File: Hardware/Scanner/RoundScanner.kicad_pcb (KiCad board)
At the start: 4 copper layers, 45 x 42.5 mm, 78 parts, among them J1 I2C ThroughHole, J3 I2C, J4 Interface, Q1 BSS138DW-7-F, U1 OPA2376xxD, U2 NAU7802SGI, U4 OPA2376xxD, U5 TLC59208FIPWR, U6 AS7341-DLGT, U7 AP7312-1833W6-7, X1 4.9152 MHz

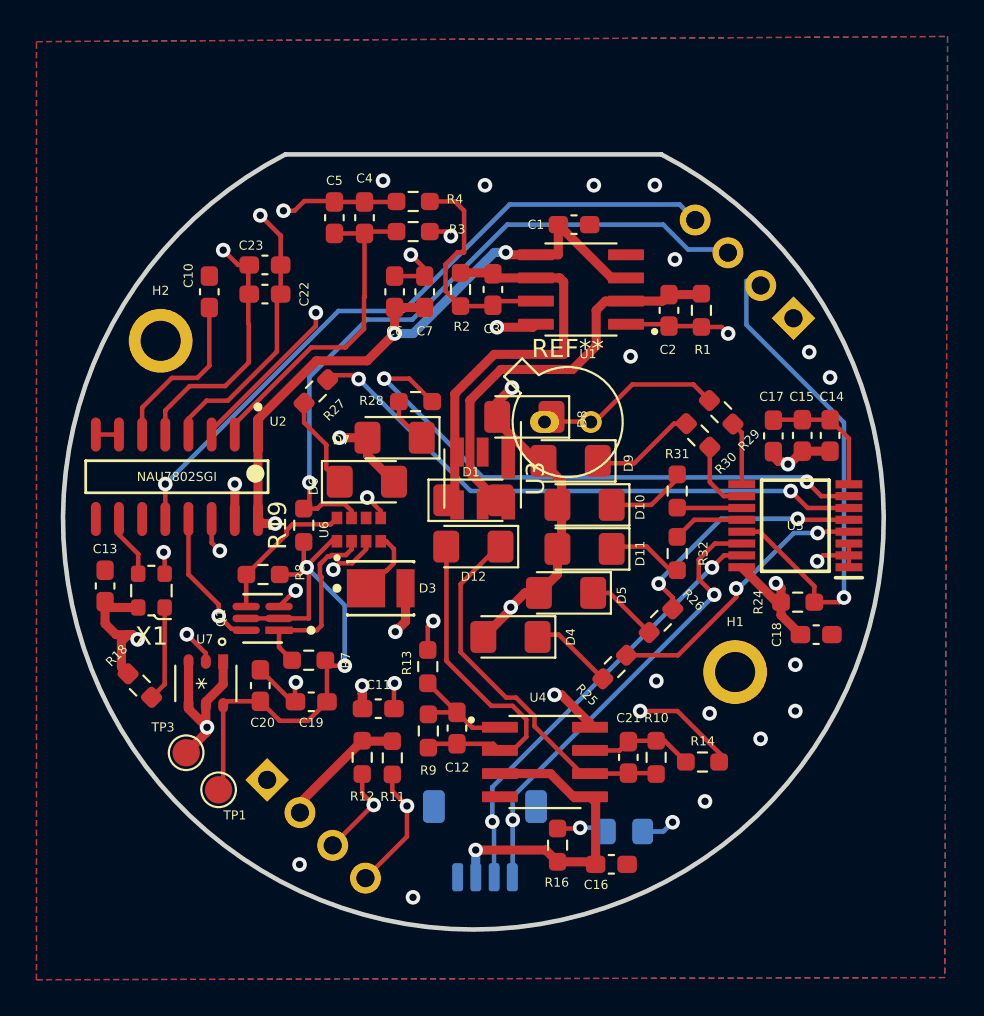
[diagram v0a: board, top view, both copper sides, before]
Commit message: lots of changes, added footprints, fixed broken schemaitcs, fixed kicad 7.0 issues
Signed-off-by: lokimetasmith <lokimail@gmail.com>
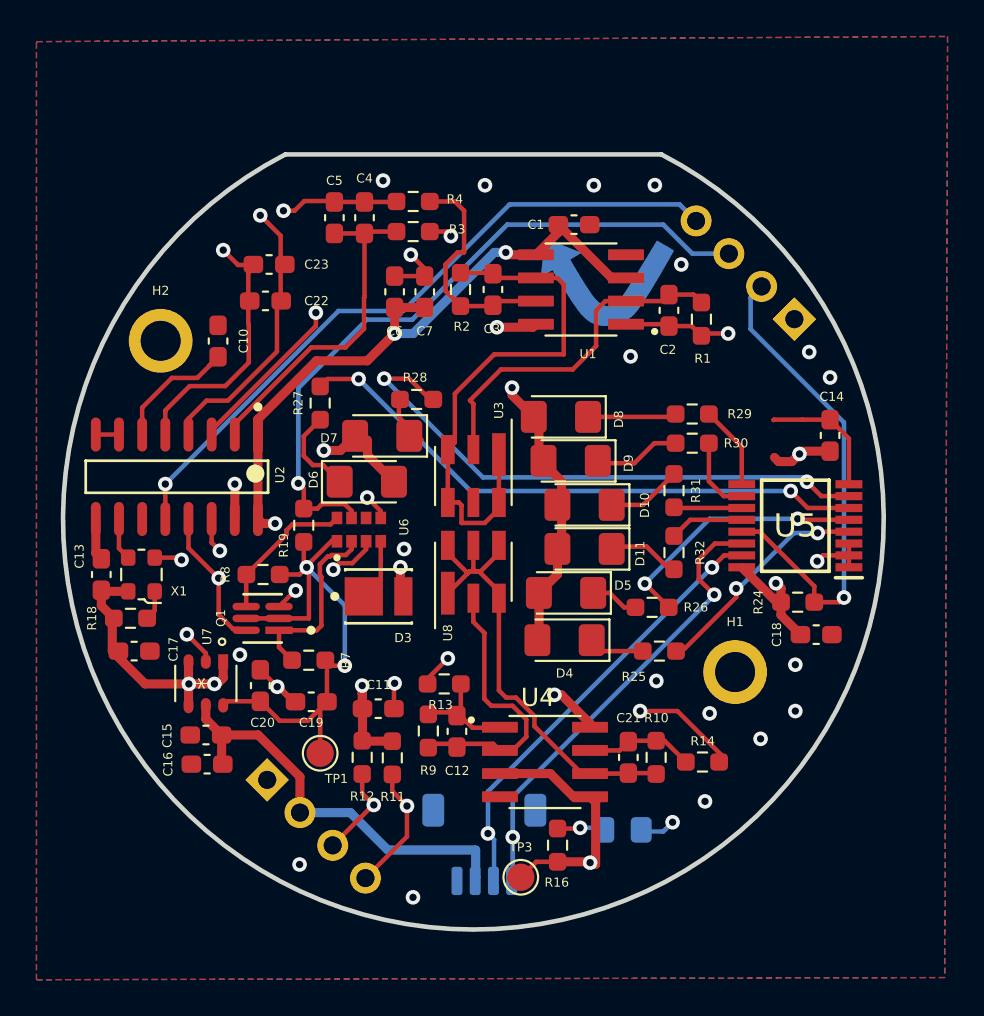
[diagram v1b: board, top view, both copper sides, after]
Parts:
- removed D1, D12: 0090-3111-185, Diode_SMD:D_1206_3216Metric_Pad1.42x1.75mm_HandSolder
- removed REF**: TO-46-2_Window, Package_TO_SOT_THT:TO-46-2_Window
- added U8: ~, MTSM2601SMF1-100:MTSM1346SMF1-100, F.Cu at (89.3, 110.2)
- moved C17 37.0 mm to (70.7, 114.6), turned to 0 degrees
- moved C15 36.6 mm to (74.6, 119.2), turned to 0 degrees
- moved C16 22.8 mm to (74.7, 120.8), turned to 0 degrees
- moved TP3 19.6 mm to (91.9, 127.0)
- moved TP1 5.92 mm to (80.9, 120.2)
- moved R18 3.73 mm to (70.5, 112.8), turned to 180 degrees
- moved D4 2.97 mm to (94.3, 114.0)
- moved C10 2.74 mm to (75.3, 97.6)
- moved R25 2.60 mm to (99.5, 114.6), turned to 180 degrees
- moved D8 2.01 mm to (94.1, 101.7)
- moved R29 1.59 mm to (101.3, 101.6), turned to 180 degrees
- moved R13 1.31 mm to (87.7, 116.4), turned to 180 degrees
- moved X1 1.04 mm to (71.1, 110.4)
- moved R26 0.88 mm to (99.1, 112.2), turned to 180 degrees
- moved D7 0.69 mm to (84.3, 102.8)
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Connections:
- net Net-(D12-A) renamed /InGaS Sensor/Anode_2
- net Net-(D12-K) renamed /InGaS Sensor/Cathode_2
- C1 pad 2: +3V3 -> +3.3V
- C11 pad 2: +3V3 -> +3.3V
- C13 pad 1: +3V3 -> +3.3V
- C14 pad 2: +3V3 -> +3.3V
- C15 pad 2: +3V3 -> VCC
- C16 pad 2: +3V3 -> VCC
- C17 pad 1: +3V3 -> +3.3V
- C18 pad 1: +3V3 -> +3.3V
- C6 pad 2: +3V3 -> +3.3V
- C7 pad 2: +3V3 -> +3.3V
- D10 pad 2: +3V3 -> +3.3V
- D11 pad 2: +3V3 -> +3.3V
- D3 pad 2: +3V3 -> +3.3V
- D4 pad 2: +3V3 -> +3.3V
- D5 pad 2: +3V3 -> +3.3V
- D6 pad 2: +3V3 -> +3.3V
- D7 pad 2: +3V3 -> +3.3V
- D8 pad 2: +3V3 -> +3.3V
- D9 pad 2: +3V3 -> +3.3V
- J1 pad 2: +3V3 -> VCC
- J3 pad 2: +3V3 -> VCC
- J4 pad 2: /Power/LED RESET -> /LED/LED_RESET
- R11 pad 1: +3V3 -> +3.3V
- R12 pad 2: +3V3 -> +3.3V
- R16 pad 1: +3V3 -> +3.3V
- R18 pad 2: +3V3 -> +3.3V
- R24 pad 1: LED RESET -> /LED/LED_RESET
- R24 pad 2: +3V3 -> +3.3V
- TP3 pad 1: +3V3 -> +3.3V
- U1 pad 3: +3V3 -> +3.3V
- U1 pad 5: +3V3 -> +3.3V
- U1 pad 8: +3V3 -> +3.3V
- U2 pad 1: +3V3 -> +3.3V
- U2 pad 15: +3V3 -> +3.3V
- U2 pad 16: +3V3 -> +3.3V
- U4 pad 3: +3V3 -> +3.3V
- U4 pad 5: +3V3 -> +3.3V
- U4 pad 8: +3V3 -> +3.3V
- U5 pad 13: LED RESET -> /LED/LED_RESET
- U5 pad 16: +3V3 -> +3.3V
- U7 pad 1: +3V3 -> +3.3V
- U7 pad 3: +3V3 -> +3.3V
- U7 pad 4: +3V3 -> +3.3V
- U7 pad 5: +3V3 -> VCC
- X1 pad 4: +3V3 -> +3.3V
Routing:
- net +3V3: track 125.9 -> 0.00 mm, vias 16 -> 0
- net +3.3V: track 0.00 -> 112.6 mm, vias 0 -> 15
- net LED RESET: track 27.4 -> 0.00 mm, vias 1 -> 0
- net /LED/LED_RESET: track 0.00 -> 27.3 mm, vias 0 -> 1
- net VCC: track 0.00 -> 22.8 mm
- net /InGaS Sensor/Cathode: track 21.6 -> 29.0 mm
- net /InGaS Sensor/Cathode_2: track 20.1 -> 25.2 mm
- net Net-(D8-K): track 9.87 -> 4.87 mm
- net Net-(X1-Tri-State): track 5.22 -> 1.65 mm
- net /InGaS Sensor/Anode_2: track 18.9 -> 15.4 mm
- net /InGaS Sensor/Anode: track 22.1 -> 18.7 mm
- net GND: track 28.6 -> 31.5 mm, vias 25 -> 27
- net Net-(U5-~{OUT0}): track 15.2 -> 12.5 mm
- net /ADC/AIN2-: track 43.1 -> 45.7 mm
- net Net-(U2-VBG): track 9.31 -> 6.80 mm
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- added copper zone on In2.Cu, net +3.3V
- removed copper zone on In2.Cu, net +3V3
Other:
- board text added: "HandheldScanner v1.1 2023-10-29"
- board text removed: "HandheldScanner v1.0 2022-12-23"

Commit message: added linear regulator for reference voltage
Signed-off-by: lokimetasmith <lokimail@gmail.com>
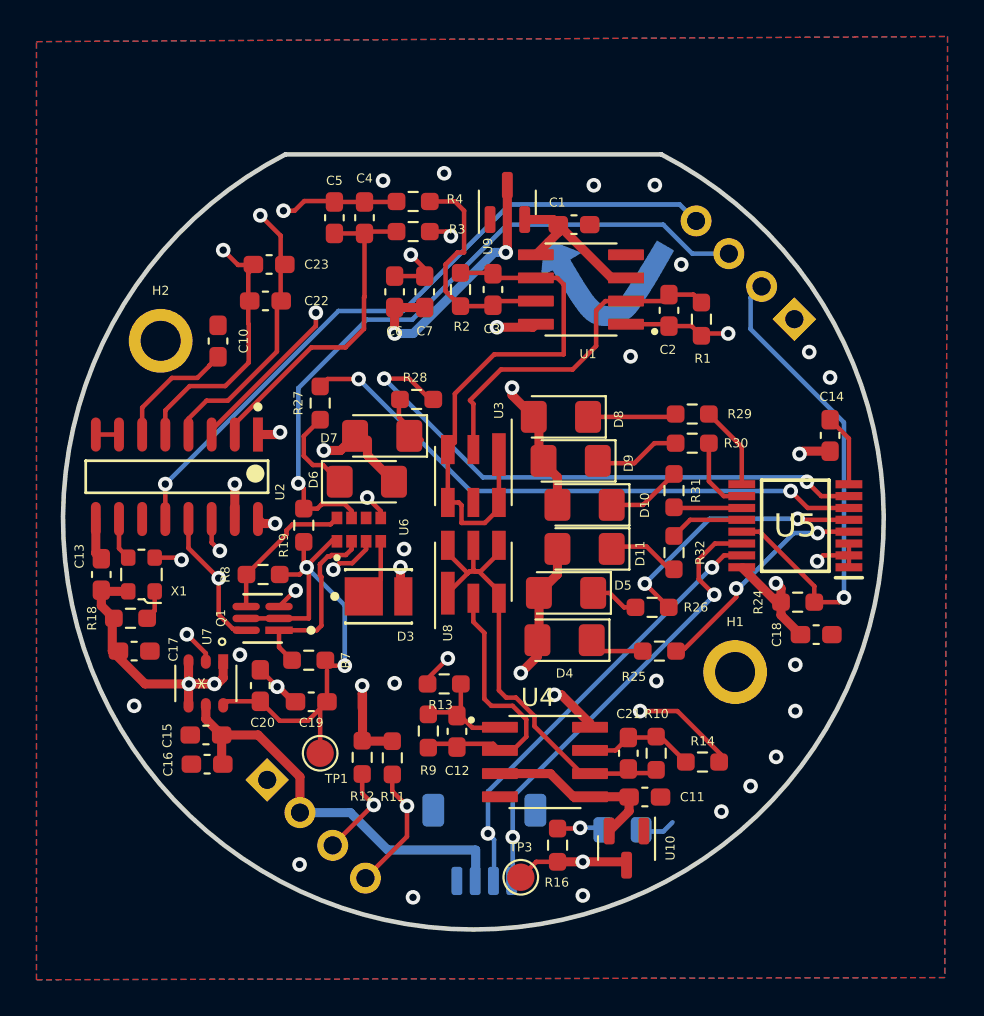
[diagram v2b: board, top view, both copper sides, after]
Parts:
- added U10: AP2127N-2.5, Package_TO_SOT_SMD:SOT-23, F.Cu at (97.7, 125.4)
- added U9: AP2127N-2.5, Package_TO_SOT_SMD:SOT-23, F.Cu at (91.1, 90.0)
- kibuzzard-6398DD41: footprint kibuzzard-6398DD41 -> PlasticScannerLibrary:kibuzzard-6398DD41
- moved C11 15.4 mm to (98.7, 122.6)
- moved C21 0.23 mm to (97.8, 120.2)
- moved R10 0.23 mm to (99.3, 120.2)
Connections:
- C1 pad 2: +3.3V -> /InGaS Sensor/Vreg1
- C11 pad 2: +3.3V -> /InGaS Sensor/Vreg2
- U1 pad 3: +3.3V -> /InGaS Sensor/Vreg1
- U1 pad 5: +3.3V -> /InGaS Sensor/Vreg1
- U4 pad 3: +3.3V -> /InGaS Sensor/Vreg2
- U4 pad 5: +3.3V -> /InGaS Sensor/Vreg2
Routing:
- net +3.3V: track 112.6 -> 79.0 mm, vias 15 -> 17
- net /InGaS Sensor/Vreg2: track 0.00 -> 9.91 mm
- net /InGaS Sensor/Vreg1: track 0.00 -> 9.04 mm
- net GND: track 31.5 -> 26.9 mm, vias 27 -> 28
- net /InGaS Sensor/Cathode_2: track 25.2 -> 23.8 mm
- net /InGaS Sensor/Anode_2: track 15.4 -> 14.4 mm

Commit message: added options for using internal adc, external adc, or 3.3v
Signed-off-by: lokimetasmith <lokimail@gmail.com>
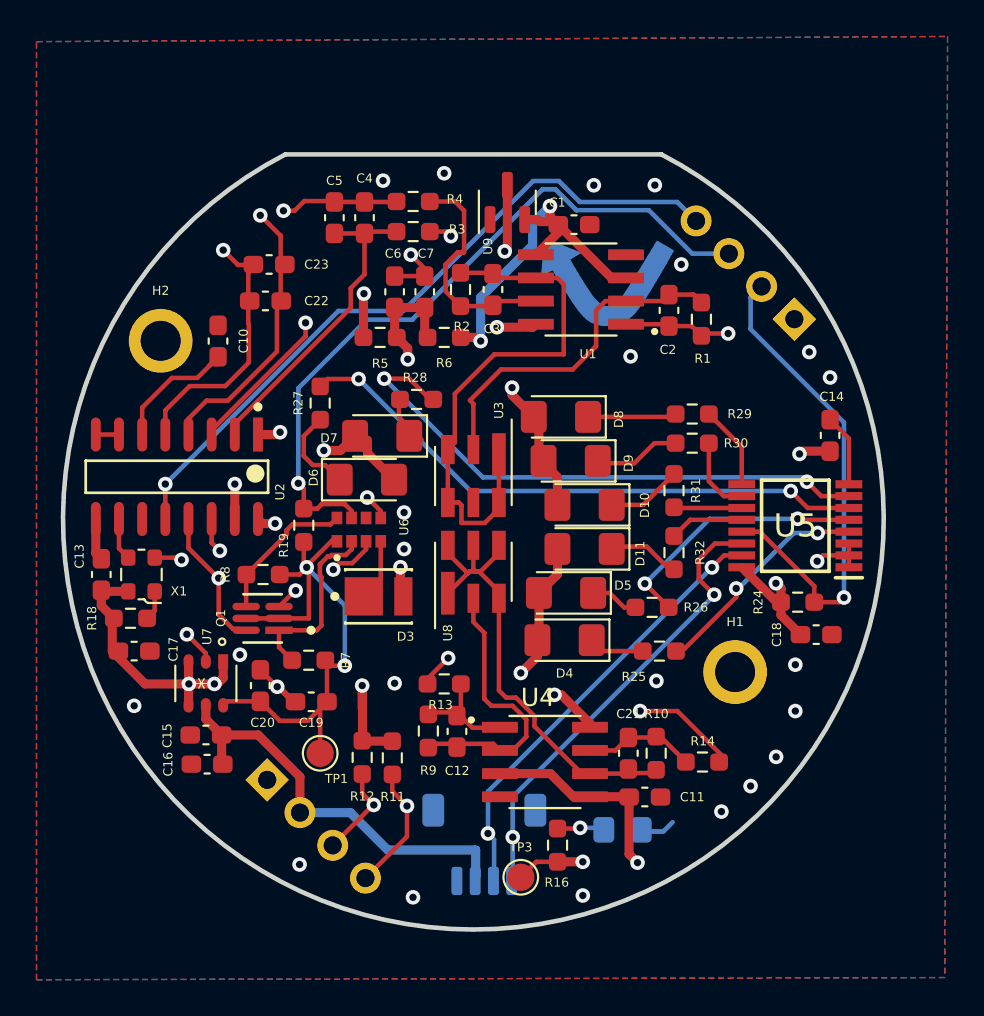
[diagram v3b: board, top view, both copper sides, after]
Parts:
- removed U10: AP2127N-2.5, Package_TO_SOT_SMD:SOT-23
- added R5: NP, Resistor_SMD:R_0603_1608Metric_Pad0.98x0.95mm_HandSolder, F.Cu at (84.2, 97.4)
- added R6: 1, Resistor_SMD:R_0603_1608Metric_Pad0.98x0.95mm_HandSolder, F.Cu at (87.7, 97.4)
- moved D6 0.11 mm to (83.4, 105.2)
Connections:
- C1 pad 2: /InGaS Sensor/Vreg1 -> VDDA
- C11 pad 2: /InGaS Sensor/Vreg2 -> VDDA
- C6 pad 2: +3.3V -> Net-(U2-AVDD/LDO)
- C7 pad 2: +3.3V -> Net-(U2-AVDD/LDO)
- U1 pad 3: /InGaS Sensor/Vreg1 -> VDDA
- U1 pad 5: /InGaS Sensor/Vreg1 -> VDDA
- U2 pad 1: +3.3V -> Net-(U2-AVDD/LDO)
- U2 pad 16: +3.3V -> Net-(U2-AVDD/LDO)
- U4 pad 3: /InGaS Sensor/Vreg2 -> VDDA
- U4 pad 5: /InGaS Sensor/Vreg2 -> VDDA
- U9 pad 2: /InGaS Sensor/Vreg1 -> VDDA
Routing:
- net VDDA: track 0.00 -> 66.0 mm, vias 0 -> 3
- net Net-(U2-AVDD/LDO): track 0.00 -> 22.0 mm, vias 0 -> 3
- net +3.3V: track 79.0 -> 65.4 mm, vias 17 -> 15
- net /InGaS Sensor/Vreg2: track 9.91 -> 0.00 mm
- net /InGaS Sensor/Vreg1: track 9.04 -> 0.00 mm
- net /MCU + IO/AS7341_INT: track 38.0 -> 39.6 mm
- net /ADC/AIN-: track 17.8 -> 16.7 mm
- net /ADC/DRDY_INT: track 37.7 -> 38.8 mm
- net GND: vias 28 -> 29

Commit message: updated pcb silkscreen date
Signed-off-by: lokimetasmith <lokimail@gmail.com>
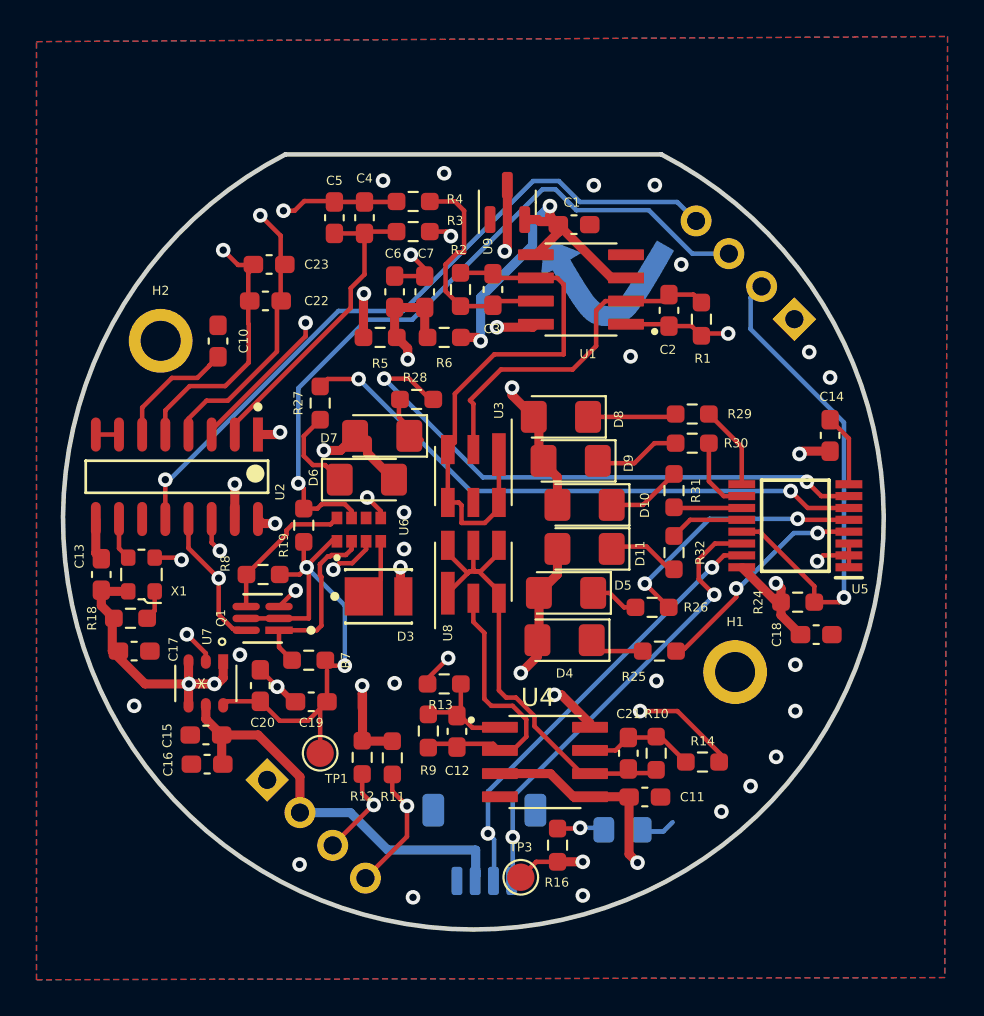
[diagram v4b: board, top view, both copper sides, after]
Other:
- board text added: "HandheldScanner v1.1 2023-11-10"
- board text removed: "HandheldScanner v1.1 2023-10-29"
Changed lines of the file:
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@@
     (property "turn off delay time" "20ns")
     (property "turn on delay time" "20ns")
-    (attr through_hole)
+    (attr smd)
     (fp_text reference "Q1" (at 2.286 0.508 90) (layer "F.SilkS")
         (effects (font (size 0.5 0.5) (thickness 0.125)) (justify right))
@@
     (property "ki_keywords" "R res resistor")
     (attr smd)
-    (fp_text reference "R2" (at -2.032 0.07 180) (layer "F.SilkS")
+    (fp_text reference "R2" (at 2.173 -0.095 180) (layer "F.SilkS")
         (effects (font (size 0.5 0.5) (thickness 0.125)))
     )
@@
     (property "ki_description" "Dual Low-Noise, Low Quiescent Current, Precision Operational Amplifier e-trim Series, SOIC-8")
     (property "ki_keywords" "dual opamp")
-    (attr through_hole)
+    (attr smd)
     (fp_text reference "U4" (at -0.385 -3.537) (layer "F.SilkS")
         (effects (font (size 1 1) (thickness 0.15)))
@@
     (property "ki_keywords" "R res resistor")
     (attr smd)
-    (fp_text reference "R8" (at 2.07 0 90) (layer "F.SilkS")
+    (fp_text reference "R8" (at 2.07 0.6 90) (layer "F.SilkS")
         (effects (font (size 0.5 0.5) (thickness 0.125)))
     )
@@
     (property "ki_description" "Dual Low-Noise, Low Quiescent Current, Precision Operational Amplifier e-trim Series, SOIC-8")
     (property "ki_keywords" "dual opamp")
-    (attr through_hole)
+    (attr smd)
     (fp_text reference "U1" (at -0.385 -3.537 180) (layer "F.SilkS")
         (effects (font (size 0.5 0.5) (thickness 0.125)))
@@
     (property "ki_keywords" "cap capacitor")
     (attr smd)
-    (fp_text reference "C1" (at 0.918 1.217 180) (layer "F.SilkS")
+    (fp_text reference "C1" (at 0.118 1.217 180) (layer "F.SilkS")
         (effects (font (size 0.5 0.5) (thickness 0.125)))
     )
@@
     (property "vault revision" "C0AC1098-4EF5-4502-9510-91D6A29A40EB")
     (attr smd)
-    (fp_text reference "U5" (at 0 0 180) (layer "F.SilkS")
-        (effects (font (size 1.27 1.27) (thickness 0.254)))
+    (fp_text reference "U5" (at -3.547 -3.473 180) (layer "F.SilkS")
+        (effects (font (size 0.5 0.5) (thickness 0.125)))
     )
     (fp_text value "TLC59208FIPWR" (at 0 0 180) (layer "F.SilkS") hide
@@
     (property "ki_keywords" "R res resistor")
     (attr smd)
-    (fp_text reference "R3" (at -2.413 0.127) (layer "F.SilkS")
+    (fp_text reference "R3" (at -2.302 0.598) (layer "F.SilkS")
         (effects (font (size 0.5 0.5) (thickness 0.125)))
     )
@@
   (gr_arc (start 99.588764 87.335) (mid 89.281 129.835) (end 78.973236 87.335)
     (stroke (width 0.25) (type solid)) (layer "Edge.Cuts"))
-  (gr_text "HandheldScanner v1.1\n2023-10-29" (at 89.281 117.475) (layer "B.SilkS")
+  (gr_text "HandheldScanner v1.1\n2023-11-10" (at 89.281 117.475) (layer "B.SilkS")
     (effects (font (size 1 1) (thickness 0.15)) (justify mirror))
   )
@@
   (segment (start 103.288898 92.776898) (end 101.285898 92.776898) (width 0.25) (layer "B.Cu") (net 9))
   (segment (start 101.285898 92.776898) (end 98.903499 90.394499) (width 0.25) (layer "B.Cu") (net 9))
-  (segment (start 72.39 107.326567) (end 72.39 105.41) (width 0.25) (layer "F.Cu") (net 10))
-  (via (at 72.39 105.41) (size 0.8) (drill 0.4) (layers "F.Cu" "B.Cu") (net 10))
+  (segment (start 72.39 107.326567) (end 72.39 105.169) (width 0.25) (layer "F.Cu") (net 10))
+  (via (at 72.39 105.169) (size 0.8) (drill 0.4) (layers "F.Cu" "B.Cu") (net 10))
+  (segment (start 100.456844 89.944844) (end 95.117132 89.944844) (width 0.25) (layer "B.Cu") (net 10))
   (segment (start 93.967287 88.794999) (end 92.555001 88.794999) (width 0.25) (layer "B.Cu") (net 10))
   (segment (start 95.117132 89.944844) (end 93.967287 88.794999) (width 0.25) (layer "B.Cu") (net 10))
+  (segment (start 72.631 105.169) (end 72.39 105.169) (width 0.25) (layer "B.Cu") (net 10))
+  (segment (start 85.431 95.919) (end 81.881 95.919) (width 0.25) (layer "B.Cu") (net 10))
   (segment (start 92.555001 88.794999) (end 85.431 95.919) (width 0.25) (layer "B.Cu") (net 10))
-  (segment (start 100.456844 89.944844) (end 95.117132 89.944844) (width 0.25) (layer "B.Cu") (net 10))
   (segment (start 101.492846 90.980846) (end 100.456844 89.944844) (width 0.25) (layer "B.Cu") (net 10))
-  (segment (start 85.431 95.919) (end 81.881 95.919) (width 0.25) (layer "B.Cu") (net 10))
-  (segment (start 81.881 95.919) (end 72.39 105.41) (width 0.25) (layer "B.Cu") (net 10))
+  (segment (start 81.881 95.919) (end 72.631 105.169) (width 0.25) (layer "B.Cu") (net 10))
   (segment (start 102.858663 120.246663) (end 100.468 117.856) (width 0.25) (layer "F.Cu") (net 11))
   (segment (start 73.72402 100.03848) (end 75.67722 100.03848) (width 0.25) (layer "F.Cu") (net 11))
